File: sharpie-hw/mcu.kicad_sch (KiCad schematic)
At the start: 36 parts, among them J2 Conn_01x03_MountingPin, J3 Conn_01x07, J4 Conn_01x07, SW1 SW_Push, SW2 SW_Push, SW3 SW_Push, U3 RP2350_60QFN, U4 W25Q128JVS, Y1 Crystal_GND24

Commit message: sharpie-hw prototype 1: complete
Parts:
- removed J2: Conn_01x03_MountingPin, symbol Connector_Generic_MountingPin:Conn_01x03_MountingPin
- removed J3, J4: Conn_01x07, symbol Connector_Generic:Conn_01x07
- added J1: Conn_01x03_MountingPin, symbol Connector_Generic_MountingPin:Conn_01x03_MountingPin
- added J2, J4: Conn_01x11, symbol Connector_Generic:Conn_01x11
- added J5, J7: Conn_01x07, symbol Connector_Generic:Conn_01x07
- added JP2: BatteryVoltageJumper, symbol Jumper:SolderJumper_2_Bridged
- added R13: 27k, symbol Device:R
- added R14: 47k, symbol Device:R
- R5: value 10k -> 50k
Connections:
- net +3.2V: now also J4.1 (Pin_1)
- net +3.3V: now also J2.10 (Pin_10)
- net B0: now also J7.5 (Pin_5)
- net B1: now also J7.6 (Pin_6)
- net BCK: now also J5.5 (Pin_5)
- net BSP: now also J5.4 (Pin_4)
- net EX_A1: now also J2.3 (Pin_3)
- net EX_A2: now also J2.4 (Pin_4)
- net EX_A3: now also J2.5 (Pin_5)
- net EX_A4: now also J2.6 (Pin_6)
- net EX_A5: now also J2.7 (Pin_7)
- net EX_A6: now also J2.8 (Pin_8)
- net EX_A7: now also J2.9 (Pin_9)
- net EX_B1: now also J4.3 (Pin_3)
- net EX_B2: now also J4.4 (Pin_4)
- net EX_B3: now also J4.5 (Pin_5)
- net EX_B4: now also J4.6 (Pin_6), R13.2, R14.1
- net EX_B5: now also J4.7 (Pin_7)
- net EX_B6: now also J4.8 (Pin_8)
- net EX_B7: now also J4.9 (Pin_9)
- net G0: now also J7.3 (Pin_3)
- net G1: now also J7.4 (Pin_4)
- net GCK: now also J5.3 (Pin_3)
- net GND: now also J1.2 (Pin_2), J1.MP (MountPin), J2.11 (Pin_11), J2.2 (Pin_2), J4.11 (Pin_11), J4.2 (Pin_2), J7.7 (Pin_7), R14.2
- net GSP: now also J5.2 (Pin_2)
- net INTB: now also J5.1 (Pin_1)
- net R0: now also J7.1 (Pin_1)
- net R1: now also J7.2 (Pin_2)
- net SWCLK: now also J1.1 (Pin_1)
- net SWDIO: now also J1.3 (Pin_3)
- net VA: now also J5.6 (Pin_6)
- net VB_VCOM: now also J5.7 (Pin_7)
- net VDD2 sw renamed 5V EN
- new net: JP2.2 (B), R13.1
- new net +5V: J4.10 (Pin_10)
- new net VCC: J2.1 (Pin_1), JP2.1 (A)
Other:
- note added: "5V*(47k/(27k+47k))=3.17V"
- note added: "Battery voltage"
- note added: "L1 must be an Abracon AOTA-B201610S3R3-101-T. Follow hardware design placement guidelines. JLC may have custom footprint for inductor."
- note added: "Place flash resistors close to chip, including R6, and place flash close to RP2350"
- note added: "Screen breakout for testing"
- note added: "USB lines should have characteristic impedance of 90 ohms, but tbh it's probably fine to just keep them fairly short."
- note added: "User LED and button"
- note added: "pull GPIO15 high in sw"
- note removed: "L1 must be an Abracon AOTA-B201610S3R3-101-T. Follow hardware design placement guidelines."
- note removed: "LED and button"
- note removed: "User LED and user button pull GPIO15 high in sw"
- moved on the sheet: C16, C19, C20, Y1

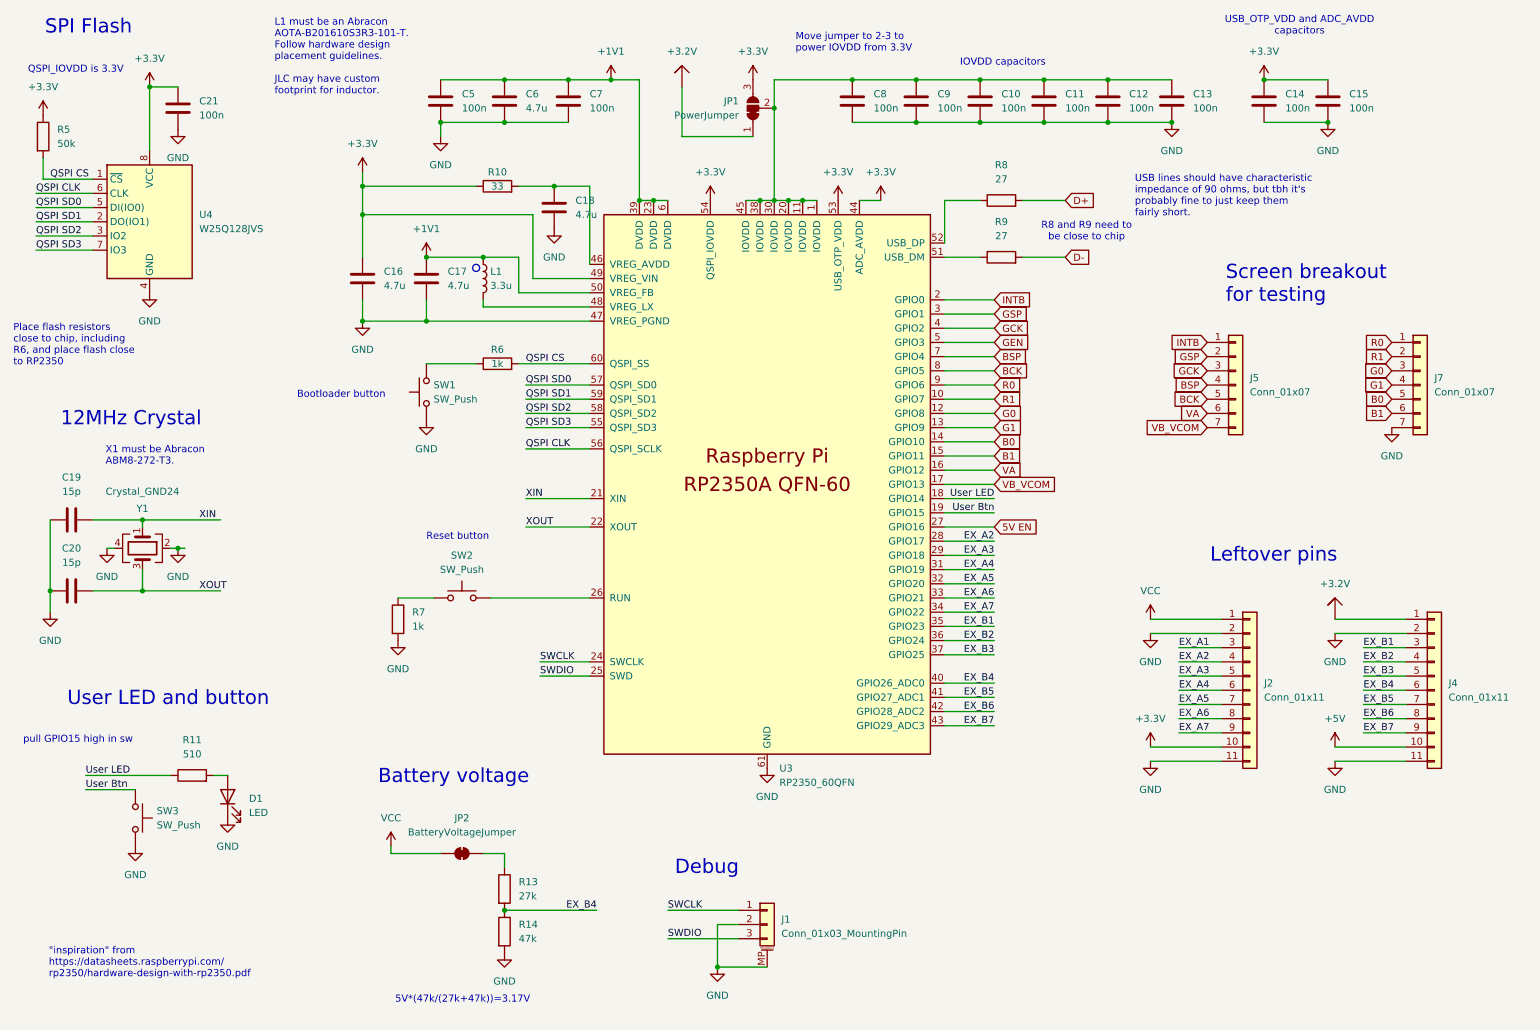
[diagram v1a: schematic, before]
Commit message: Finalize schematic, start PCB, configure manufacturing parameters, and start placing RP2350 components.
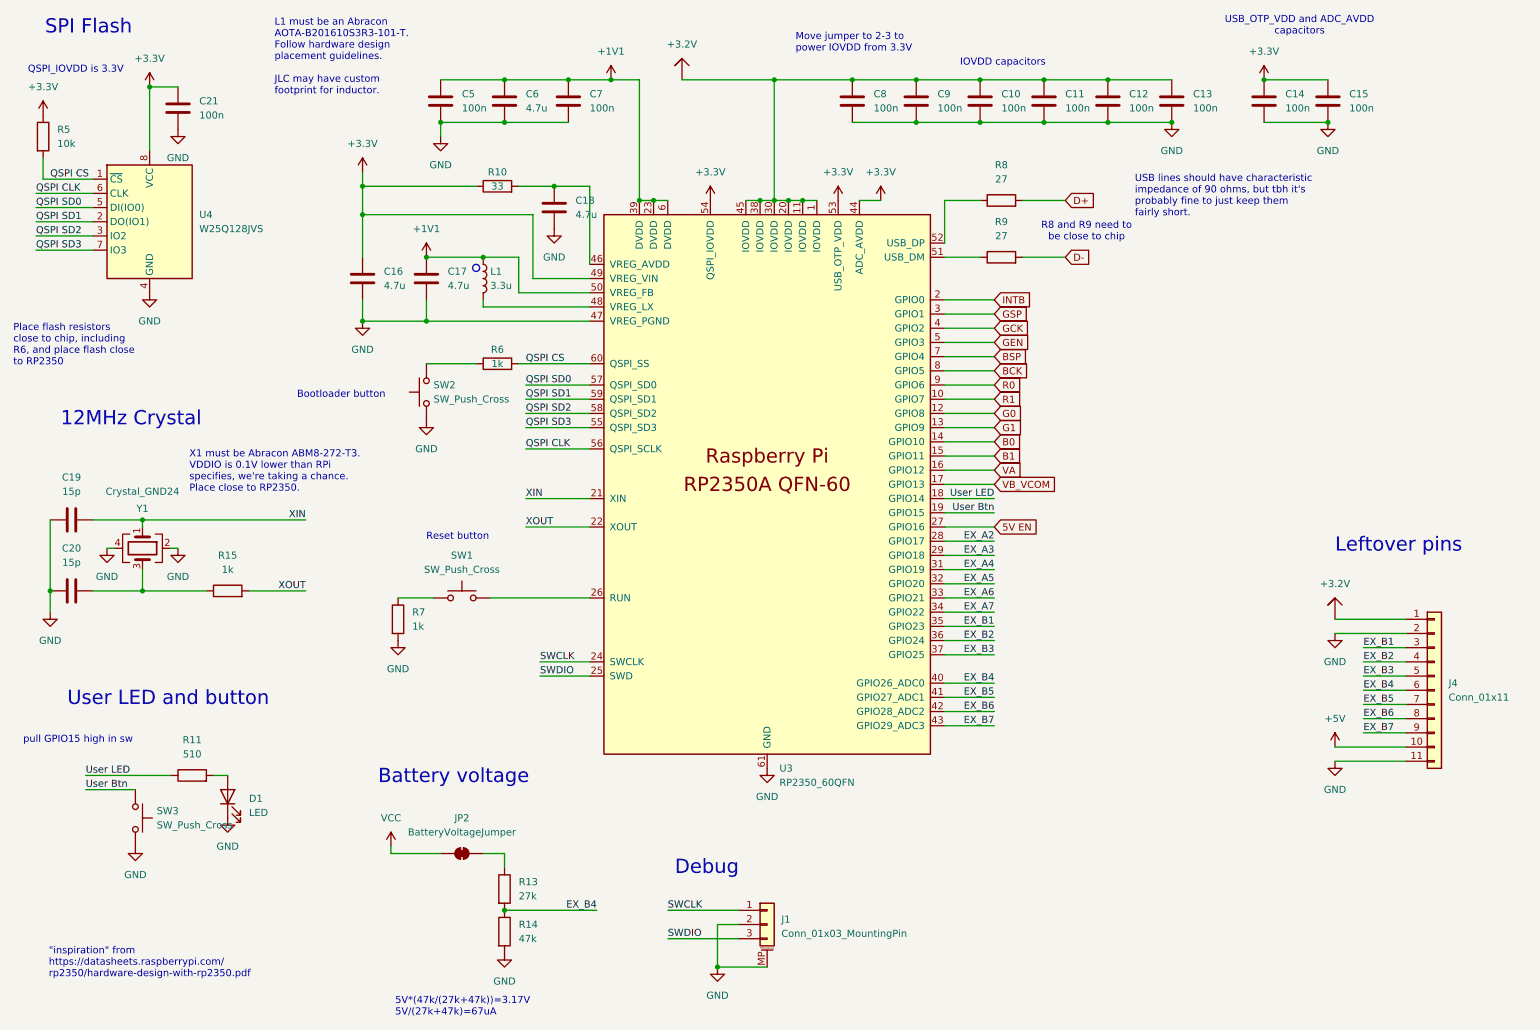
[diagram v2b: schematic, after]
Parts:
- removed J2: Conn_01x11, symbol Connector_Generic:Conn_01x11
- removed J5, J7: Conn_01x07, symbol Connector_Generic:Conn_01x07
- removed JP1: PowerJumper, symbol Jumper:SolderJumper_3_Bridged12
- removed SW1, SW2, SW3: SW_Push, symbol Switch:SW_Push
- removed U3: RP2350_60QFN, RP2350_60QFN_minimal:RP2350-QFN-60-1EP_7x7_P0.4mm_EP3.4x3.4mm_ThermalVias, symbol MCU_RaspberryPi_RP2350:RP2350_60QFN
- added R15: 1k, Resistor_SMD:R_0402_1005Metric, symbol Device:R
- added SW1, SW2, SW3: SW_Push_Cross, Sharpie:KEY-SMD_4P-L4.2-W3.2-P2.20-LS4.6, symbol sharpie-hw:SW_Push_Cross
- added U3: RP2350_60QFN, Sharpie:RP2350-QFN-60-1EP_7x7_P0.4mm_EP3.4x3.4mm_ThermalVias, symbol sharpie-hw:RP2350_60QFN
- C10, C11, C12, C13, C14, C15, C5, C8, C9: footprint (none) -> Capacitor_SMD:C_0402_1005Metric; JLCPCB Part # (none) -> C1525
- C16, C17: footprint (none) -> Sharpie:C_0402_1005Metric_small_pads; JLCPCB Part # (none) -> C23733
- C18, C6: footprint (none) -> Capacitor_SMD:C_0402_1005Metric; JLCPCB Part # (none) -> C23733
- C19, C20: footprint (none) -> Capacitor_SMD:C_0402_1005Metric; JLCPCB Part # (none) -> C107110
- C21: footprint (none) -> Capacitor_SMD:C_0402_1005Metric; JLCPCB Part # (none) -> C49678
- C7: footprint (none) -> Capacitor_SMD:C_0402_1005Metric; JLCBPCB Part # (none) -> C1525
- D1: footprint (none) -> LED_SMD:LED_0805_2012Metric
- J1: footprint (none) -> Connector_JST:JST_SH_SM03B-SRSS-TB_1x03-1MP_P1.00mm_Horizontal; JLCPCB Part # (none) -> C160403
- J4: footprint (none) -> Connector_PinHeader_2.54mm:PinHeader_1x11_P2.54mm_Vertical
- JP2: footprint (none) -> Jumper:SolderJumper-2_P1.3mm_Bridged_Pad1.0x1.5mm
- L1: footprint (none) -> Sharpie:L_pol_2016; JLCPCB Part # (none) -> C42411119
- R10, R11: footprint (none) -> Resistor_SMD:R_0402_1005Metric
- R13: footprint (none) -> Resistor_SMD:R_0402_1005Metric; JLCPCB Part # (none) -> C17593
- R14: footprint (none) -> Resistor_SMD:R_0402_1005Metric; JLCPCB Part # (none) -> C29252
- R5: value 50k -> 10k; footprint (none) -> Resistor_SMD:R_0402_1005Metric; JLCPCB Part # (none) -> C25531
- R6: footprint (none) -> Resistor_SMD:R_0402_1005Metric; JLCPCB Part # (none) -> C11702
- R7: footprint (none) -> Resistor_SMD:R_0402_1005Metric; JLCPCB Part # (none) -> C25623
- R8, R9: footprint (none) -> Resistor_SMD:R_0402_1005Metric; JLCPCB Part # (none) -> C25156
- U4: JLCPCB Part # (none) -> C97521
- Y1: footprint (none) -> Crystal:Crystal_SMD_3225-4Pin_3.2x2.5mm; JLCPCB Part # (none) -> C20625731
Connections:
- net +1V1: now also U3.23 (DVDD), U3.39 (DVDD), U3.50 (VREG_FB), U3.6 (DVDD)
- net +3.2V: now also C10.1, C11.1, C12.1, C13.1, C8.1, C9.1, U3.1 (IOVDD), U3.11 (IOVDD), U3.20 (IOVDD), U3.30 (IOVDD), U3.38 (IOVDD), U3.45 (IOVDD)
- net +3.3V: now also U3.44 (ADC_AVDD), U3.49 (VREG_VIN), U3.53 (USB_OTP_VDD), U3.54 (QSPI_IOVDD)
- net 5V EN: now also U3.27 (GPIO16)
- net B0: now also U3.14 (GPIO10)
- net B1: now also U3.15 (GPIO11)
- net BCK: now also U3.8 (GPIO5)
- net BSP: now also U3.7 (GPIO4)
- net EX_A2: now also U3.28 (GPIO17)
- net EX_A3: now also U3.29 (GPIO18)
- net EX_A4: now also U3.31 (GPIO19)
- net EX_A5: now also U3.32 (GPIO20)
- net EX_A6: now also U3.33 (GPIO21)
- net EX_A7: now also U3.34 (GPIO22)
- net EX_B1: now also U3.35 (GPIO23)
- net EX_B2: now also U3.36 (GPIO24)
- net EX_B3: now also U3.37 (GPIO25)
- net EX_B4: now also U3.40 (GPIO26_ADC0)
- net EX_B5: now also U3.41 (GPIO27_ADC1)
- net EX_B6: now also U3.42 (GPIO28_ADC2)
- net EX_B7: now also U3.43 (GPIO29_ADC3)
- net G0: now also U3.12 (GPIO8)
- net G1: now also U3.13 (GPIO9)
- net GCK: now also U3.4 (GPIO2)
- net GEN: now also U3.5 (GPIO3)
- net GND: now also SW2.1, SW2.2, SW3.3 (2), SW3.4, U3.47 (VREG_PGND), U3.61 (GND)
- net GSP: now also U3.3 (GPIO1)
- net INTB: now also U3.2 (GPIO0)
- net QSPI CLK: now also U3.56 (QSPI_SCLK)
- net QSPI CS: now also U3.60 (QSPI_SS)
- net QSPI SD0: now also U3.57 (QSPI_SD0)
- net QSPI SD1: now also U3.59 (QSPI_SD1)
- net QSPI SD2: now also U3.58 (QSPI_SD2)
- net QSPI SD3: now also U3.55 (QSPI_SD3)
- net R0: now also U3.9 (GPIO6)
- net R1: now also U3.10 (GPIO7)
- net SWCLK: now also U3.24 (SWCLK)
- net SWDIO: now also U3.25 (SWD)
- net User Btn: now also SW3.1, SW3.2, U3.19 (GPIO15)
- net User LED: now also U3.18 (GPIO14)
- net VA: now also U3.16 (GPIO12)
- net VB_VCOM: now also U3.17 (GPIO13)
- net XIN: now also U3.21 (XIN)
- net XOUT: now also R15.2, U3.22 (XOUT); no longer C20.2, Y1.3
- net at C18.1, R10.2: now also U3.46 (VREG_AVDD)
- net at R6.1: now also SW2.3 (2), SW2.4
- net at R7.1: now also SW1.1, SW1.2
- net at L1.2: now also U3.48 (VREG_LX)
- net at R9.1: now also U3.51 (USB_DM)
- net at R8.1: now also U3.52 (USB_DP)
- new net: C20.2, R15.1, Y1.3
- new net: SW1.3 (2), SW1.4, U3.26 (RUN)
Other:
- note added: "5V*(47k/(27k+47k))=3.17V 5V/(27k+47k)=67uA"
- note added: "X1 must be Abracon ABM8-272-T3. VDDIO is 0.1V lower than RPi specifies, we're taking a chance. Place close to RP2350."
- note removed: "5V*(47k/(27k+47k))=3.17V"
- note removed: "Screen breakout for testing"
- note removed: "X1 must be Abracon ABM8-272-T3."

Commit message: Modify FPC footprint, add alternate USB-C footprint, and commit final (before review) design.
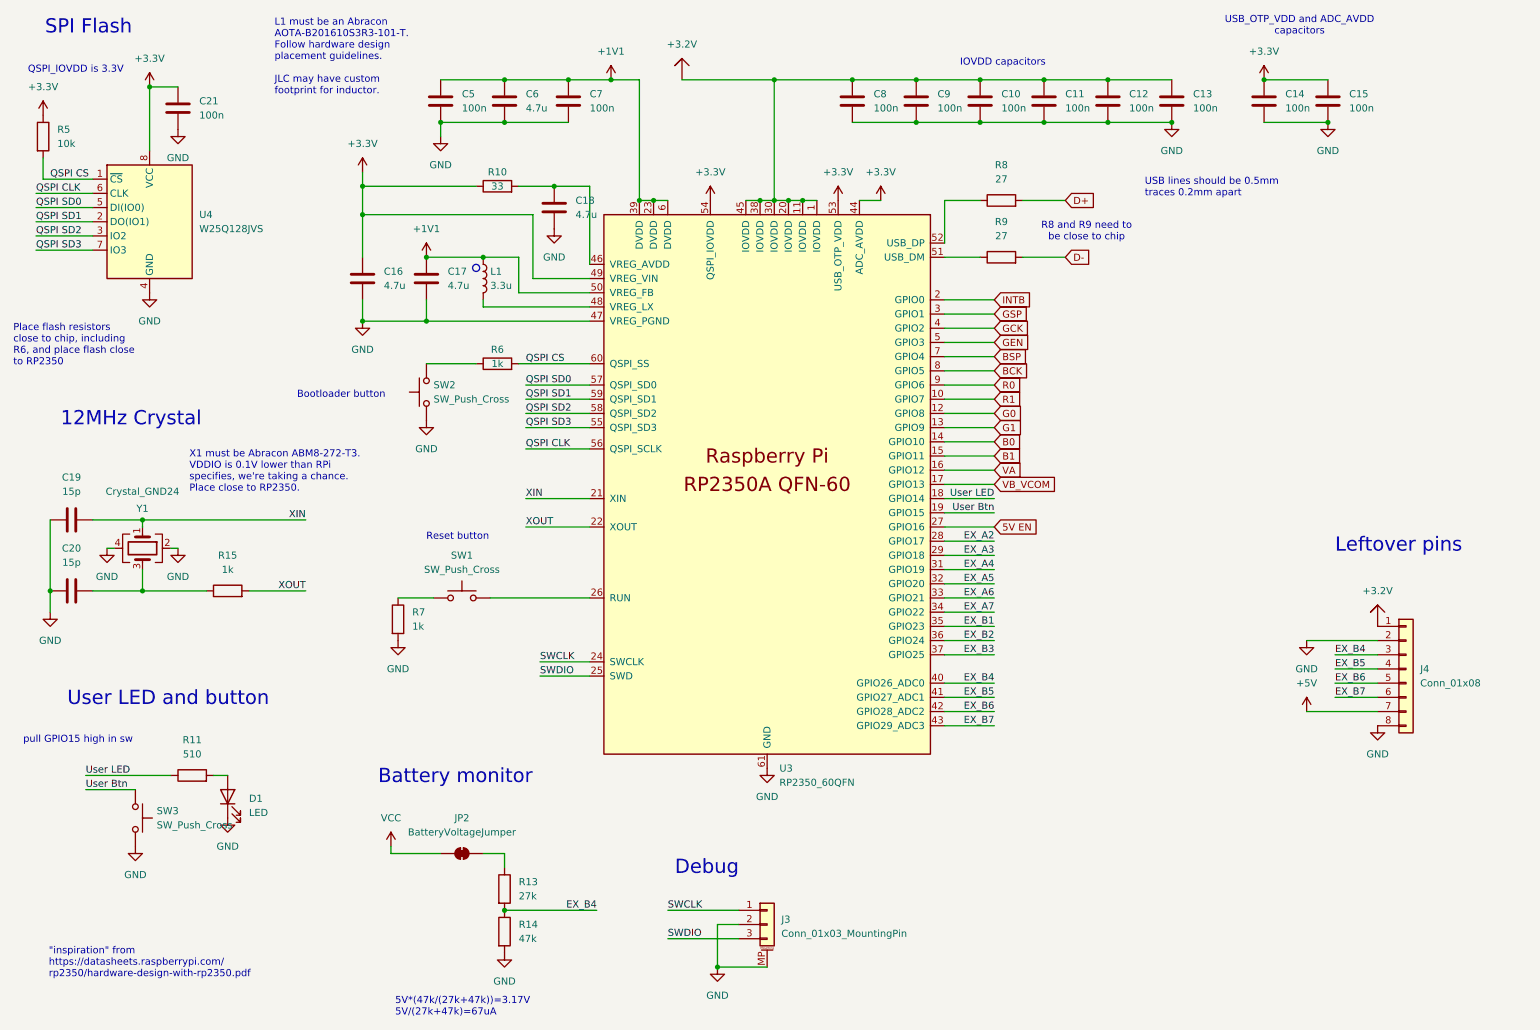
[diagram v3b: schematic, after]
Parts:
- removed J4: Conn_01x11, Connector_PinHeader_2.54mm:PinHeader_1x11_P2.54mm_Vertical, symbol Connector_Generic:Conn_01x11
- added J4: Conn_01x08, Connector_PinHeader_2.54mm:PinHeader_1x08_P2.54mm_Vertical, symbol Connector_Generic:Conn_01x08
- renumbered J1 to J3
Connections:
- net +3.2V: now also J4.1 (Pin_1)
- net +5V: now also J4.7 (Pin_7)
- net EX_B4: now also J4.3 (Pin_3)
- net EX_B5: now also J4.4 (Pin_4)
- net EX_B6: now also J4.5 (Pin_5)
- net EX_B7: now also J4.6 (Pin_6)
- net GND: now also J4.2 (Pin_2), J4.8 (Pin_8)
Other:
- note added: "Battery monitor"
- note added: "USB lines should be 0.5mm traces 0.2mm apart"
- note removed: "Battery voltage"
- note removed: "Move jumper to 2-3 to power IOVDD from 3.3V"
- note removed: "USB lines should have characteristic impedance of 90 ohms, but tbh it's probably fine to just keep them fairly short."

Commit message: Add all JLCPCB part numbers and some PCB silkscreens.
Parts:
- C19, C20: JLCPCB Part # C107110 -> C325460
- C21: JLCPCB Part # C49678 -> C1525
- C7: JLCBPCB Part # C1525 -> (none); JLCPCB Part # (none) -> C1525
- D1: JLCPCB Part # (none) -> C2292
- R10: JLCPCB Part # (none) -> C25105
- R11: JLCPCB Part # (none) -> C25123
- R13: JLCPCB Part # C17593 -> C25551
- R7: JLCPCB Part # C25623 -> C11702
- SW1, SW2, SW3: JLCPCB Part # (none) -> C116501
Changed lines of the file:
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@@
 			)
 		)
+		(property "JLCPCB Part #" "C25123"
+			(at 45.72 152.4 0)
+			(effects
+				(font
+					(size 1.27 1.27)
+				)
+				(hide yes)
+			)
+		)
 		(pin "2"
 		)
@@
 			)
 		)
-		(property "JLCPCB Part #" "C107110"
+		(property "JLCPCB Part #" "C325460"
 			(at 24.13 106.68 90)
 			(effects
@@
 			)
 		)
+		(property "JLCPCB Part #" "C2292"
+			(at 52.07 156.21 0)
+			(effects
+				(font
+					(size 1.27 1.27)
+				)
+				(hide yes)
+			)
+		)
 		(pin "1"
 		)
@@
 			)
 		)
-		(property "JLCPCB Part #" "C49678"
+		(property "JLCPCB Part #" "C1525"
 			(at 43.18 33.02 0)
 			(effects
@@
 			)
 		)
+		(property "JLCPCB Part #" "C116501"
+			(at 93.98 120.65 0)
+			(effects
+				(font
+					(size 1.27 1.27)
+				)
+				(hide yes)
+			)
+		)
 		(pin "1"
 		)
@@
 			)
 		)
-		(property "JLCPCB Part #" "C17593"
+		(property "JLCPCB Part #" "C25551"
 			(at 101.6 172.72 0)
 			(effects
@@
 			)
 		)
-		(property "JLCPCB Part #" "C107110"
+		(property "JLCPCB Part #" "C325460"
 			(at 24.13 119.38 90)
 			(effects
@@
 			)
 		)
+		(property "JLCPCB Part #" "C116501"
+			(at 87.63 83.82 0)
+			(effects
+				(font
+					(size 1.27 1.27)
+				)
+				(hide yes)
+			)
+		)
 		(pin "1"
 		)
@@
 			)
 		)
-		(property "JLCBPCB Part #" "C1525"
+		(property "JLCPCB Part #" "C1525"
 			(at 113.03 31.75 0)
 			(effects
@@
 			)
 		)
-		(property "JLCPCB Part #" "C25623"
+		(property "JLCPCB Part #" "C11702"
 			(at 82.55 124.46 0)
 			(effects
@@
 			)
 		)
+		(property "JLCPCB Part #" "C116501"
+			(at 35.56 160.02 0)
+			(effects
+				(font
+					(size 1.27 1.27)
+				)
+				(hide yes)
+			)
+		)
 		(pin "3"
 		)
@@
 			(at 100.33 46.99 0)
 			(effects
+				(font
+					(size 1.27 1.27)
+				)
+				(hide yes)
+			)
+		)
+		(property "JLCPCB Part #" "C25105"
+			(at 100.33 46.99 0)
+			(effects
